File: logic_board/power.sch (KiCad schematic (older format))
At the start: 22 parts, among them J4 Amphenol 124015, J5 Batt, SW5 Power, U4 TPS562200, U5 BQ24090DGQR

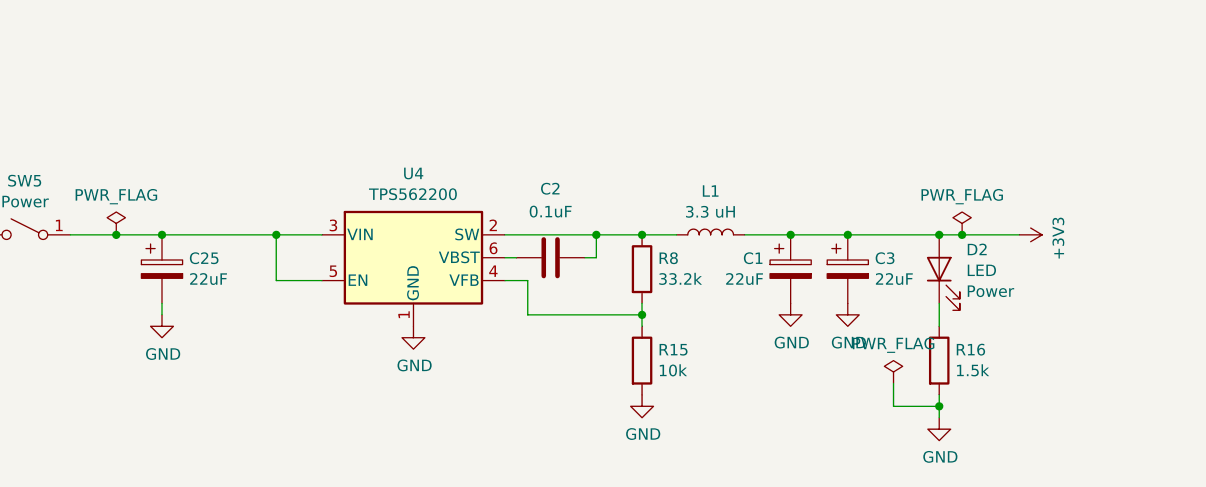
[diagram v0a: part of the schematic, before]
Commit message: Switch from switching to LDO regulator
This simplifies the design and reduces part count. Since the typical
use case is only a few hours of usage, the difference in efficiency
doesn't seem to justify the additional complexity.
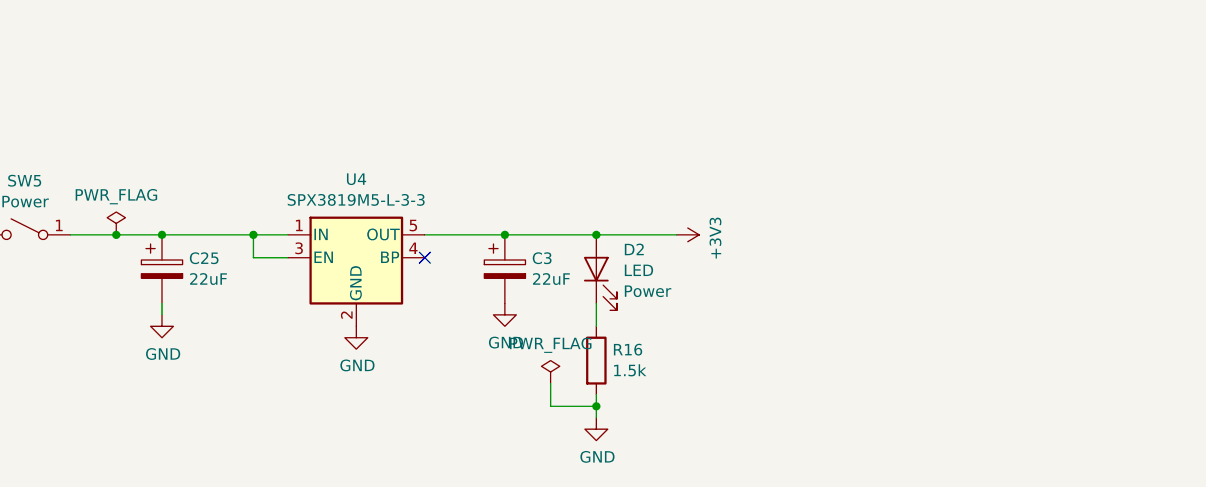
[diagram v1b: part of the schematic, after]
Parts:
- removed C1: 22uF, Capacitors_SMD:CP_Elec_6.3x4.5, symbol Device:CP
- removed C2: 0.1uF, Capacitors_SMD:C_0402, symbol Device:C
- removed L1: 3.3 uH, Inductors_SMD:L_Taiyo-Yuden_NR-60xx_HandSoldering, symbol Device:L
- removed R15: 10k, Resistors_SMD:R_0402, symbol Device:R
- removed R8: 33.2k, Resistors_SMD:R_0402, symbol Device:R
- removed U4: TPS562200, TO_SOT_Packages_SMD:SOT-23-6_Handsoldering, symbol Regulator_Switching:TPS562200
- added U4: SPX3819M5-L-3-3, TO_SOT_Packages_SMD:SOT-23-5_HandSoldering, symbol Regulator_Linear:SPX3819M5-L-3-3
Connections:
- net +3V3: now also U4.5 (OUT)
- net GND: now also U4.2 (GND)
- net at C25.1, SW5.1 (A): now also U4.1 (IN), U4.3 (EN)
- no-connect marks 4 -> 5
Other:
- moved on the sheet: C3, D2, R16
